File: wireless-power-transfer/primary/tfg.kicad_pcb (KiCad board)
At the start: 2 copper layers, 160 x 100 mm, 55 parts, among them J1 CONN_01X06, J2 Screw_Terminal_1x02, J3 BARREL_JACK, Q1 IRLB8721PBF, Q2 IRLB8721PBF, Q3 IRLB8721PBF, Q4 IRLB8721PBF, U1 PIC18F45K20-I/PT, U2 IR2110, U3 IR2110, U4 R-78E15, U5 R-78E3.3, U6 XBEE_Wi-Fi

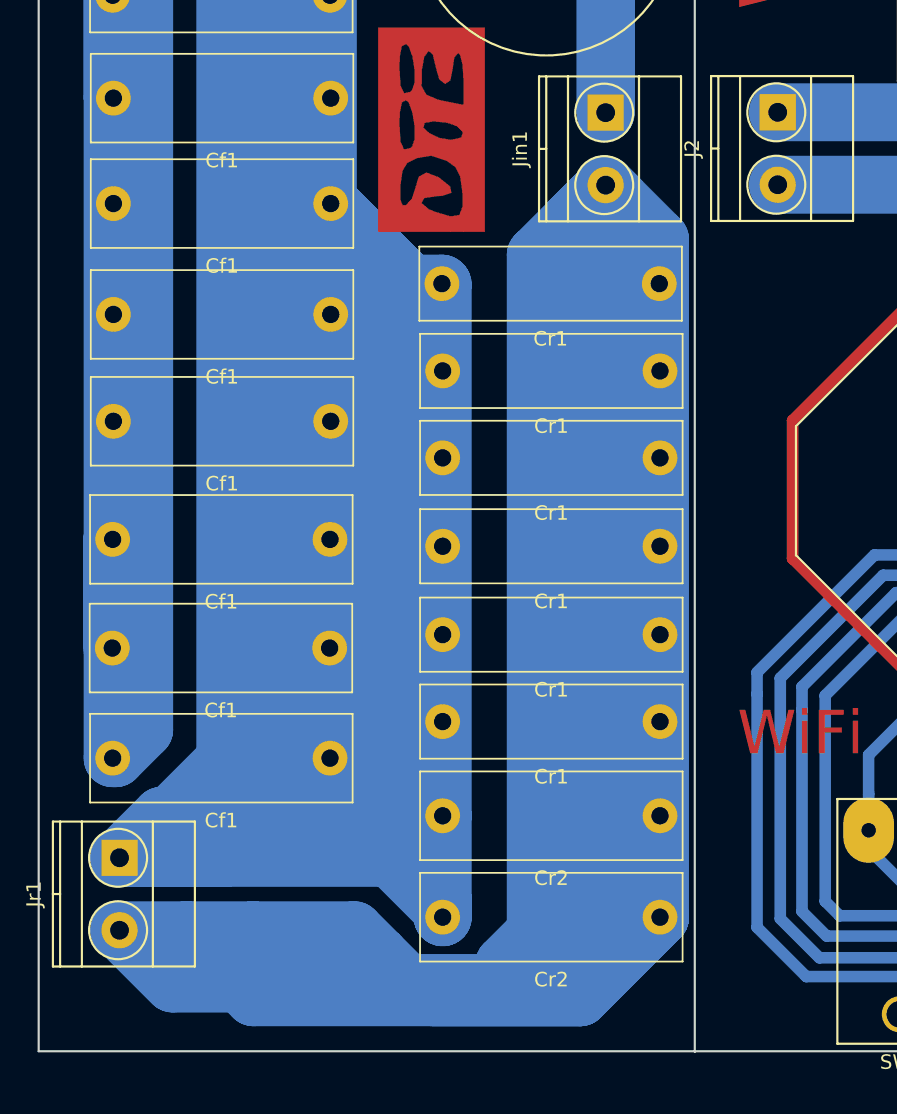
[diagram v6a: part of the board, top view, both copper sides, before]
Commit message: Added a second connector for resonant coil of the primary.
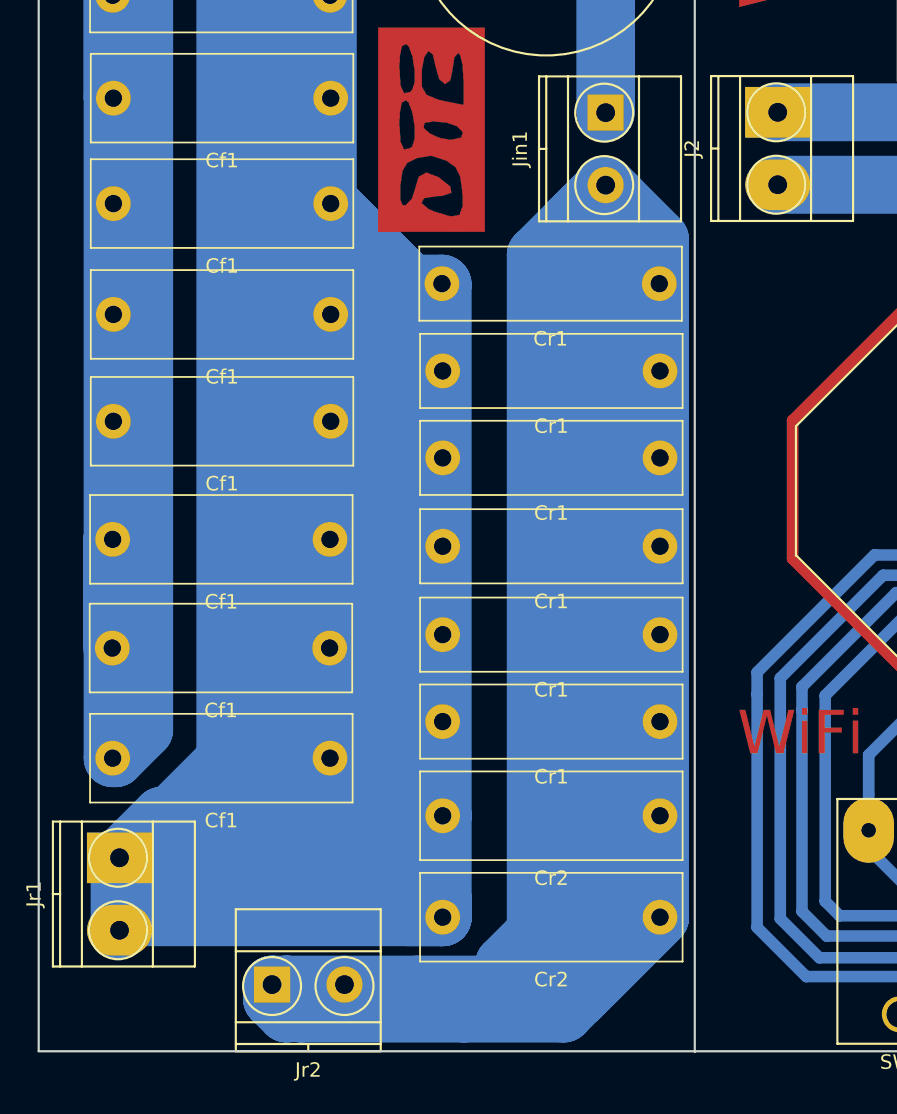
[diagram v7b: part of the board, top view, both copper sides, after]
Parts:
- added Jr2: Screw_Terminal_1x02, Connectors_Terminal_Blocks:TerminalBlock_Pheonix_MKDS1.5-2pol, F.Cu at (74.0, 121.0)
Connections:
- Jr1 pad 2: Net-(Cr1-Pad1) -> Net-(Cf1-Pad1)
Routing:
- net Net-(Cr1-Pad1): track 370.0 -> 312.5 mm
- net Net-(Cf1-Pad1): track 479.9 -> 531.4 mm
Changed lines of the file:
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@@
 (kicad_pcb (version 4) (host pcbnew 4.0.6)
   (general
-    (links 122)
+    (links 124)
     (no_connects 24)
-    (area 56.3 23.8 223.280001 127.727)
+    (area 57.819999 25.526999 217.970001 125.725001)
     (thickness 1.6)
     (drawings 21)
-    (tracks 578)
+    (tracks 583)
     (zones 0)
-    (modules 55)
+    (modules 56)
     (nets 77)
   )
@@
   )
   (setup
-    (last_trace_width 0.8)
+    (last_trace_width 4)
     (user_trace_width 0.45)
     (user_trace_width 0.8)
@@
     (mod_text_size 1 1)
     (mod_text_width 0.15)
-    (pad_size 4 5.5)
-    (pad_drill 1.5)
+    (pad_size 3.5 4.5)
+    (pad_drill 1.3)
     (pad_to_mask_clearance 0.2)
     (aux_axis_origin 0 0)
@@
     (fp_line (start 7.5 -5.2) (end -2.5 -5.2) (layer F.SilkS) (width 0.15))
     (fp_line (start -2.5 -5.2) (end -2.5 4.6) (layer F.SilkS) (width 0.15))
-    (pad 1 thru_hole rect (at 0 0 270) (size 2.5 2.5) (drill 1.3) (layers *.Cu *.Mask)
+    (pad 1 thru_hole rect (at 0 0 270) (size 3.5 4.5) (drill 1.3) (layers *.Cu *.Mask)
       (net 72 "Net-(F1-Pad1)"))
-    (pad 2 thru_hole circle (at 5 0 270) (size 2.5 2.5) (drill 1.3) (layers *.Cu *.Mask)
+    (pad 2 thru_hole oval (at 5 0 270) (size 3.5 4.5) (drill 1.3) (layers *.Cu *.Mask)
       (net 7 "Net-(Cboot2-Pad2)"))
     (model Terminal_Blocks.3dshapes/TerminalBlock_Pheonix_MKDS1.5-2pol.wrl
@@
     (fp_line (start 7.5 -5.2) (end -2.5 -5.2) (layer F.SilkS) (width 0.15))
     (fp_line (start -2.5 -5.2) (end -2.5 4.6) (layer F.SilkS) (width 0.15))
-    (pad 1 thru_hole rect (at 0 0 270) (size 2.5 2.5) (drill 1.3) (layers *.Cu *.Mask)
+    (pad 1 thru_hole rect (at 0 0 270) (size 3.5 4.5) (drill 1.3) (layers *.Cu *.Mask)
       (net 73 "Net-(Cf1-Pad1)"))
-    (pad 2 thru_hole circle (at 5 0 270) (size 2.5 2.5) (drill 1.3) (layers *.Cu *.Mask)
-      (net 75 "Net-(Cr1-Pad1)"))
+    (pad 2 thru_hole oval (at 5 0 270) (size 3.5 4.5) (drill 1.3) (layers *.Cu *.Mask)
+      (net 73 "Net-(Cf1-Pad1)"))
     (model Terminal_Blocks.3dshapes/TerminalBlock_Pheonix_MKDS1.5-2pol.wrl
       (at (xyz 0.0984 0 0))
@@
       (xy -5.06238 -0.684596) (xy -5.48829 -0.179191) (xy -5.653176 0.208022) (xy -5.985372 1.328457)
       (xy -7.055555 1.328457) (xy -7.055555 -3.681159) (xy 7.055556 -3.681159) (xy 7.055556 3.681159)) (layer F.Cu) (width 0.01))
+  )
+  (module Connectors_Terminal_Blocks:TerminalBlock_Pheonix_MKDS1.5-2pol (layer F.Cu)
+    (at 74 121)
+    (descr "2-way 5mm pitch terminal block, Phoenix MKDS series")
+    (fp_text reference Jr2 (at 2.5 5.9) (layer F.SilkS)
+      (effects (font (size 1 1) (thickness 0.15)))
+    )
+    (fp_text value Screw_Terminal_1x02 (at 2.5 -6.6) (layer F.Fab)
+      (effects (font (size 1 1) (thickness 0.15)))
+    )
+    (fp_line (start -2.7 -5.4) (end 7.7 -5.4) (layer F.CrtYd) (width 0.05))
+    (fp_line (start -2.7 4.8) (end -2.7 -5.4) (layer F.CrtYd) (width 0.05))
+    (fp_line (start 7.7 4.8) (end -2.7 4.8) (layer F.CrtYd) (width 0.05))
+    (fp_line (start 7.7 -5.4) (end 7.7 4.8) (layer F.CrtYd) (width 0.05))
+    (fp_line (start 2.5 4.1) (end 2.5 4.6) (layer F.SilkS) (width 0.15))
+    (fp_circle (center 5 0.1) (end 3 0.1) (layer F.SilkS) (width 0.15))
+    (fp_circle (center 0 0.1) (end 2 0.1) (layer F.SilkS) (width 0.15))
+    (fp_line (start -2.5 2.6) (end 7.5 2.6) (layer F.SilkS) (width 0.15))
+    (fp_line (start -2.5 -2.3) (end 7.5 -2.3) (layer F.SilkS) (width 0.15))
+    (fp_line (start -2.5 4.1) (end 7.5 4.1) (layer F.SilkS) (width 0.15))
+    (fp_line (start -2.5 4.6) (end 7.5 4.6) (layer F.SilkS) (width 0.15))
+    (fp_line (start 7.5 4.6) (end 7.5 -5.2) (layer F.SilkS) (width 0.15))
+    (fp_line (start 7.5 -5.2) (end -2.5 -5.2) (layer F.SilkS) (width 0.15))
+    (fp_line (start -2.5 -5.2) (end -2.5 4.6) (layer F.SilkS) (width 0.15))
+    (pad 1 thru_hole rect (at 0 0) (size 2.5 2.5) (drill 1.3) (layers *.Cu *.Mask)
+      (net 75 "Net-(Cr1-Pad1)"))
+    (pad 2 thru_hole circle (at 5 0) (size 2.5 2.5) (drill 1.3) (layers *.Cu *.Mask)
+      (net 75 "Net-(Cr1-Pad1)"))
+    (model Terminal_Blocks.3dshapes/TerminalBlock_Pheonix_MKDS1.5-2pol.wrl
+      (at (xyz 0.0984 0 0))
+      (scale (xyz 1 1 1))
+      (rotate (xyz 0 0 0))
+    )
   )
   (gr_text "TFG SDVP" (at 78 28) (layer F.Cu)
@@
   (segment (start 108.9 60.8) (end 119.025 60.8) (width 4) (layer B.Cu) (net 72))
   (segment (start 119.025 60.8) (end 122.175 57.65) (width 4) (layer B.Cu) (net 72))
+  (segment (start 85.775 116.35) (end 83.35 116.35) (width 4) (layer B.Cu) (net 73))
+  (segment (start 65.725 115) (end 63.475 117.25) (width 4) (layer B.Cu) (net 73))
+  (segment (start 82 115) (end 65.725 115) (width 4) (layer B.Cu) (net 73))
+  (segment (start 83.35 116.35) (end 82 115) (width 4) (layer B.Cu) (net 73))
+  (segment (start 63.475 117.25) (end 63.475 112.25) (width 4) (layer B.Cu) (net 73))
+  (segment (start 85.775 116.35) (end 64.375 116.35) (width 4) (layer B.Cu) (net 73))
+  (segment (start 64.375 116.35) (end 63.475 117.25) (width 4) (layer B.Cu) (net 73))
   (segment (start 85.775 116.35) (end 85.775 115.875) (width 4) (layer B.Cu) (net 73))
   (segment (start 85.775 115.875) (end 82.15 112.25) (width 4) (layer B.Cu) (net 73))
@@
   (segment (start 74.7 37.55) (end 77.85 34.4) (width 4) (layer B.Cu) (net 73))
   (segment (start 63.475 112.25) (end 67.25 112.25) (width 4) (layer B.Cu) (net 73))
+  (segment (start 74.125 105.375) (end 74.7 105.375) (width 4) (layer B.Cu) (net 73))
   (segment (start 67.25 112.25) (end 74.125 105.375) (width 4) (layer B.Cu) (net 73))
-  (segment (start 74.125 105.375) (end 74.7 105.375) (width 4) (layer B.Cu) (net 73))
   (segment (start 74.7 105.375) (end 78 105.375) (width 4) (layer B.Cu) (net 73))
   (segment (start 63.475 112.25) (end 70.825 112.25) (width 4) (layer B.Cu) (net 73))
@@
   (segment (start 63 105.375) (end 63 34.55) (width 4) (layer B.Cu) (net 74))
   (segment (start 63 34.55) (end 62.85 34.4) (width 4) (layer B.Cu) (net 74))
-  (segment (start 72.675 117.25) (end 79.675 117.25) (width 4) (layer B.Cu) (net 75))
+  (segment (start 87.25 123) (end 94.125 123) (width 4) (layer B.Cu) (net 75))
+  (segment (start 94.125 123) (end 100.775 116.35) (width 4) (layer B.Cu) (net 75) (status 800000))
+  (segment (start 76 123) (end 74 121) (width 4) (layer B.Cu) (net 75) (status 800000))
+  (segment (start 87.25 123) (end 76 123) (width 4) (layer B.Cu) (net 75))
+  (segment (start 74 121) (end 74 122) (width 4) (layer B.Cu) (net 75) (status C00000))
+  (segment (start 74 122) (end 75 123) (width 4) (layer B.Cu) (net 75) (status 400000))
+  (segment (start 75 123) (end 75 121) (width 4) (layer B.Cu) (net 75) (status 800000))
+  (segment (start 84 121) (end 89.95 121) (width 4) (layer B.Cu) (net 75))
+  (segment (start 89.95 121) (end 89.075 121.875) (width 4) (layer B.Cu) (net 75))
+  (segment (start 79 121) (end 84 121) (width 4) (layer B.Cu) (net 75) (status 400000))
+  (segment (start 89.075 121.875) (end 95.25 121.875) (width 4) (layer B.Cu) (net 75))
+  (segment (start 74 121) (end 75 121) (width 4) (layer B.Cu) (net 75) (status C00000))
+  (segment (start 75 121) (end 79 121) (width 4) (layer B.Cu) (net 75) (status C00000))
   (segment (start 96.2 120.925) (end 100.775 116.35) (width 4) (layer B.Cu) (net 75))
-  (segment (start 83.35 120.925) (end 96.2 120.925) (width 4) (layer B.Cu) (net 75))
-  (segment (start 79.675 117.25) (end 83.35 120.925) (width 4) (layer B.Cu) (net 75))
   (segment (start 90.025 120.925) (end 90.025 119.575) (width 4) (layer B.Cu) (net 75))
   (segment (start 92.2 70.65) (end 97.025 65.825) (width 4) (layer B.Cu) (net 75))
@@
   (segment (start 97.85 66.65) (end 97.025 65.825) (width 4) (layer B.Cu) (net 75))
   (segment (start 100.775 116.35) (end 97.85 116.35) (width 4) (layer B.Cu) (net 75))
-  (segment (start 67.15 120.925) (end 63.475 117.25) (width 4) (layer B.Cu) (net 75))
   (segment (start 93.275 120.925) (end 94.525 120.925) (width 4) (layer B.Cu) (net 75))
   (segment (start 94.525 120.925) (end 90.025 120.925) (width 4) (layer B.Cu) (net 75))
-  (segment (start 90.025 120.925) (end 67.15 120.925) (width 4) (layer B.Cu) (net 75))
   (segment (start 97.85 116.35) (end 93.275 120.925) (width 4) (layer B.Cu) (net 75))
-  (segment (start 63.475 117.25) (end 63.5 117.25) (width 4) (layer B.Cu) (net 75))
-  (segment (start 63.5 117.25) (end 67.05 120.8) (width 4) (layer B.Cu) (net 75))
-  (segment (start 72.725 121.875) (end 95.25 121.875) (width 4) (layer B.Cu) (net 75))
-  (segment (start 71.65 120.8) (end 72.725 121.875) (width 4) (layer B.Cu) (net 75))
-  (segment (start 67.05 120.8) (end 71.65 120.8) (width 4) (layer B.Cu) (net 75))
   (segment (start 95.25 121.875) (end 100.775 116.35) (width 4) (layer B.Cu) (net 75))
-  (segment (start 85.05 121.875) (end 95.25 121.875) (width 4) (layer B.Cu) (net 75))
-  (segment (start 63.475 117.25) (end 68.1 117.25) (width 4) (layer B.Cu) (net 75))
-  (segment (start 68.1 117.25) (end 72.675 117.25) (width 4) (layer B.Cu) (net 75))
-  (segment (start 74.4 118.975) (end 81.4 118.975) (width 4) (layer B.Cu) (net 75))
-  (segment (start 72.675 117.25) (end 74.4 118.975) (width 4) (layer B.Cu) (net 75))
   (segment (start 100.775 116.35) (end 100.775 69.575) (width 4) (layer B.Cu) (net 75))
   (segment (start 100.775 69.575) (end 97.025 65.825) (width 4) (layer B.Cu) (net 75))
